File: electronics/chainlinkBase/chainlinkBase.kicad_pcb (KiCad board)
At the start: 2 copper layers, 107 parts, among them J1 Power In, J10 UART, J11 Output, J12 Output, J13 Output, J14 CHANNEL, J2 CHANNEL, J3 CHANNEL, J4 RELAY, J5 CHANNEL, J6 CHANNEL, J7 RS485, J8 RS485, J9 Logic Power Out, SW1 SW_DIP_x04, U1 AP7361C-33E, U10 INA219BxD, U11 VN7007ALH, U12 VN7007ALH, U13 SN74LV1T34DBV, U14 SP485, U15 INA219BxD, U16 VN7007ALH, U17 SN74LV1T34DBV, U2 TPL7407L, U3 INA219BxD, U4 INA219BxD, U5 VN7007ALH, U6 VN7007ALH, U7 TTGO_TDisplay, U8 MCP23017_SS, U9 INA219BxD

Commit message: Single channel layout
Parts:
- removed C10, C11, C12, C15, C16, C23, C5, C6, C7, C8, C9: 0.1uF, Capacitor_SMD:C_0805_2012Metric
- removed D1, D12, D13, D14, D15, D16, D2, D3, D4, D5: Red, LED_SMD:LED_0805_2012Metric
- removed D6, D7: WS2812B, LED_SMD:LED_WS2812B_PLCC4_5.0x5.0mm_P3.2mm
- removed F1, F2, F3, F4, F5: Fuse Holder BK-6013, BK-6013:BK-6013
- removed J1: Power In, ScrewTerminals:EB147A-02-D
- removed J10: UART, ScrewTerminals:C72334_WJ500V-5.08-3P
- removed J11, J12, J13: Output, ScrewTerminals:EB147A-02-D
- removed J14, J2, J3, J5, J6: CHANNEL, ScrewTerminals:EB147A-02-D
- removed J7, J8: RS485, ScrewTerminals:EB147A-02-D
- removed J9: Logic Power Out, ScrewTerminals:EB147A-02-D
- removed R1, R14, R15, R2, R24: 0.01R 1% 1W, Resistor_SMD:R_0612_1632Metric
- removed R10, R20, R21, R27, R9: 220, Resistor_SMD:R_0805_2012Metric
- removed R11, R12, R22, R23, R28: 1k, Resistor_SMD:R_0805_2012Metric
- removed R16, R17, R18, R19, R25, R26, R3, R4, R7, R8: 15k, Resistor_SMD:R_0805_2012Metric
- removed R29, R30, R31, R32, R33: 2k, Resistor_SMD:R_0805_2012Metric
- removed SW1: SW_DIP_x04, Button_Switch_SMD:SW_DIP_SPSTx04_Slide_Omron_A6S-410x_W8.9mm_P2.54mm
- removed U1: AP7361C-33E, Package_TO_SOT_SMD:SOT-223-3_TabPin2
- removed U10, U15, U3, U4, U9: INA219BxD, Package_SO:SOIC-8_3.9x4.9mm_P1.27mm
- removed U11, U12, U16, U5, U6: VN7007ALH, VN7007ALHTR:VN7007ALHTR
- removed U13, U17: SN74LV1T34DBV, Package_TO_SOT_SMD:SOT-23-5
- removed U14: SP485, Package_SO:SOIC-8_3.9x4.9mm_P1.27mm
- removed U8: MCP23017_SS, Package_SO:SSOP-28_5.3x10.2mm_P0.65mm
- added C101: 47uF, Capacitor_SMD:CP_Elec_6.3x5.4, F.Cu at (123.8, 127.6)
- added C104: 47uF, Capacitor_SMD:CP_Elec_6.3x5.4, F.Cu at (123.8, 148.6)
- added C113: 0.1uF, Capacitor_SMD:C_0805_2012Metric, F.Cu at (150.5, 45.1)
- added C201: 0.1uF, Capacitor_SMD:C_0805_2012Metric, F.Cu at (171.4, 47.0)
- added C202: 0.1uF, Capacitor_SMD:C_0805_2012Metric, F.Cu at (174.6, 26.0)
- added D101: WS2812B, LED_SMD:LED_WS2812B_PLCC4_5.0x5.0mm_P3.2mm, F.Cu at (126.4, 165.7)
- added D102: WS2812B, LED_SMD:LED_WS2812B_PLCC4_5.0x5.0mm_P3.2mm, F.Cu at (226.8, 48.5)
- added D107: 2A 500mV, Diode_SMD:D_SOD-128, F.Cu at (129.5, 45.7)
- added D201: Red, LED_SMD:LED_0805_2012Metric, F.Cu at (191.8, 41.9)
- added D202: Red, LED_SMD:LED_0805_2012Metric, F.Cu at (191.8, 29.2)
- added F201: Fuse Holder BK-6013, BK-6013:BK-6013, F.Cu at (181.6, 47.0)
- added H101: MountingHole_Pad, MountingHole:MountingHole_3.2mm_M3_ISO7380_Pad, F.Cu at (105.4, 20.3)
- added H102: MountingHole_Pad, MountingHole:MountingHole_3.2mm_M3_ISO7380_Pad, F.Cu at (193.0, 20.3)
- added H103: MountingHole_Pad, MountingHole:MountingHole_3.2mm_M3_ISO7380_Pad, F.Cu at (193.0, 195.6)
- added H104: MountingHole_Pad, MountingHole:MountingHole_3.2mm_M3_ISO7380_Pad, F.Cu at (104.1, 168.9)
- added J101: Power In, ScrewTerminals:Generic-5.08-2P, F.Cu at (110.5, 40.6)
- added J103: Power In, ScrewTerminals:Generic-5.08-2P, F.Cu at (110.5, 27.9)
- added J104: RS485, ScrewTerminals:Generic-5.08-2P, F.Cu at (109.9, 105.4)
- added J105: RS485, ScrewTerminals:Generic-5.08-2P, F.Cu at (109.9, 115.6)
- added J106: Logic Power Out, ScrewTerminals:Generic-5.08-2P, F.Cu at (110.5, 128.3)
- added J107: UART, ScrewTerminals:Generic-5.08-3P, F.Cu at (109.9, 90.2)
- added J108: Output, ScrewTerminals:Generic-5.08-2P, F.Cu at (110.5, 141.0)
- added J109: Output, ScrewTerminals:Generic-5.08-2P, F.Cu at (110.5, 151.1)
- added J110: Output, ScrewTerminals:Generic-5.08-2P, F.Cu at (110.5, 161.3)
- added J201: CHANNEL, ScrewTerminals:Generic-5.08-2P, F.Cu at (184.2, 38.1)
- added JP101: LEDs, Connector_PinHeader_2.54mm:PinHeader_1x02_P2.54mm_Vertical, F.Cu at (188.0, 21.6)
- added R201: 0.01R 1% 1W, Resistor_SMD:R_0612_1632Metric, F.Cu at (174.0, 38.1)
- added R202: 2k, Resistor_SMD:R_0805_2012Metric, F.Cu at (191.8, 44.5)
- added R203: 15k, Resistor_SMD:R_0805_2012Metric, F.Cu at (184.2, 28.6)
- added R204: 15k, Resistor_SMD:R_0805_2012Metric, F.Cu at (179.7, 26.0)
- added R205: 2k, Resistor_SMD:R_0805_2012Metric, F.Cu at (191.8, 26.7)
- added R206: 1k, Resistor_SMD:R_0805_2012Metric, F.Cu at (179.7, 28.6)
- added SW101: SW_DIP_x04, Button_Switch_SMD:SW_DIP_SPSTx04_Slide_Omron_A6S-410x_W8.9mm_P2.54mm, F.Cu at (110.5, 77.5)
- added U101: AP7361C-33E, Package_TO_SOT_SMD:SOT-223-3_TabPin2, F.Cu at (123.8, 137.2)
- added U103: Buck, Buck:BuckModule, F.Cu at (136.5, 25.4)
- added U105: MCP23017_SS, Package_SO:SSOP-28_5.3x10.2mm_P0.65mm, F.Cu at (122.6, 74.3)
- added U106: SN74LV1T34DBV, Package_TO_SOT_SMD:SOT-23-5, F.Cu at (125.7, 109.2)
- added U107: SP485, Package_SO:SOIC-8_3.9x4.9mm_P1.27mm, F.Cu at (132.1, 97.2)
- added U108: SN74LV1T34DBV, Package_TO_SOT_SMD:SOT-23-5, F.Cu at (132.9, 166.1)
- added U201: INA219BxD, Package_SO:SOIC-8_3.9x4.9mm_P1.27mm, F.Cu at (166.4, 45.7)
- added U202: VN7007ALH, VN7007ALHTR:VN7007ALHTR, F.Cu at (168.9, 31.1)
- J102: renamed from J4; footprint ScrewTerminals:EB147A-02-D -> ScrewTerminals:Generic-5.08-2P
- moved C106 223.5 mm to (257.0, 109.2)
- moved C111 223.5 mm to (263.4, 93.8)
- moved C102 209.3 mm to (264.8, 74.3)
- moved C103 209.3 mm to (241.8, 93.8)
- moved C105 209.3 mm to (269.2, 75.7)
- moved C107 209.3 mm to (252.3, 89.2)
- moved C108 209.3 mm to (264.8, 77.3)
- moved C109 209.3 mm to (239.0, 102.8)
- moved C110 209.3 mm to (260.9, 80.3)
- moved C112 209.3 mm to (239.0, 99.8)
- moved D103 209.3 mm to (253.9, 76.7)
- moved D104 209.3 mm to (245.5, 76.7)
- moved D105 209.3 mm to (255.3, 68.4)
- moved R101 209.3 mm to (261.2, 89.3)
- moved R102 209.3 mm to (247.9, 102.8)
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- renumbered C2 to C102, C3 to C103, C13 to C105, C14 to C106, C17 to C107, C18 to C108, C19 to C109, C20 to C110, C21 to C111, C22 to C112, D8 to D103, D9 to D104, D10 to D105, D11 to D106, R5 to R101, R6 to R102, R13 to R103, U2 to U102, U7 to U104
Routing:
- net /OUT0_EN: track 0.00 -> 49.4 mm
- net GND: track 0.00 -> 36.6 mm, vias 0 -> 3
- net /LED_GND: track 0.00 -> 36.4 mm
- net Net-(D201-Pad2): track 0.00 -> 29.4 mm
- net +3V3: track 0.00 -> 26.5 mm
- net /PowerChannel0/POWER_MONITORED: track 0.00 -> 22.7 mm, vias 0 -> 30
- net Net-(D105-Pad2): track 0.00 -> 19.8 mm
- net /SCL: track 0.00 -> 18.5 mm
- net /SDA: track 0.00 -> 17.7 mm
- net Net-(R203-Pad1): track 0.00 -> 9.95 mm
- net +5V: track 0.00 -> 9.56 mm
- net (no net): track 0.00 -> 9.31 mm
- net /PowerChannel0/POWER_OUT: track 0.00 -> 8.26 mm
- net Net-(R204-Pad2): track 0.00 -> 6.02 mm
- net Net-(R206-Pad2): track 0.00 -> 5.16 mm
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- added copper zone on B.Cu, net (none)
- added copper zone on F.Cu, net /PowerChannel0/POWER_IN
- added copper zone on F.Cu, net /PowerChannel0/POWER_MONITORED
- added copper zone on F.Cu, net /PowerChannel0/POWER_OUT
- added copper zone on B.Cu, net GND
- added copper zone on F.Cu, net Net-(D201-Pad2)
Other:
- board outline added: 94.6 x 182.2 mm
- rule trace_min: 0.2 -> 0.16
- board text added: "Channel 0"
- board text added: "In"
- board text added: "LEDs"
- board text added: "Out"

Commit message: Lots of layout and routing
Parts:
- added C114: 0.1uF, Capacitor_SMD:C_0805_2012Metric, F.Cu at (47.6, 81.9)
- added C301: 0.1uF, Capacitor_SMD:C_0805_2012Metric, F.Cu at (99.1, 87.6)
- added C302: 0.1uF, Capacitor_SMD:C_0805_2012Metric, F.Cu at (102.2, 66.7)
- added C401: 0.1uF, Capacitor_SMD:C_0805_2012Metric, F.Cu at (99.1, 120.0)
- added C402: 0.1uF, Capacitor_SMD:C_0805_2012Metric, F.Cu at (102.2, 99.1)
- added C501: 0.1uF, Capacitor_SMD:C_0805_2012Metric, F.Cu at (99.1, 152.4)
- added C502: 0.1uF, Capacitor_SMD:C_0805_2012Metric, F.Cu at (102.2, 131.4)
- added C601: 0.1uF, Capacitor_SMD:C_0805_2012Metric, F.Cu at (99.1, 184.8)
- added C602: 0.1uF, Capacitor_SMD:C_0805_2012Metric, F.Cu at (102.2, 163.8)
- added D301: Red, LED_SMD:LED_0805_2012Metric, F.Cu at (119.4, 82.5)
- added D302: Red, LED_SMD:LED_0805_2012Metric, F.Cu at (119.4, 69.8)
- added D401: Red, LED_SMD:LED_0805_2012Metric, F.Cu at (119.4, 114.9)
- added D402: Red, LED_SMD:LED_0805_2012Metric, F.Cu at (119.4, 102.2)
- added D501: Red, LED_SMD:LED_0805_2012Metric, F.Cu at (119.4, 147.3)
- added D502: Red, LED_SMD:LED_0805_2012Metric, F.Cu at (119.4, 134.6)
- added D601: Red, LED_SMD:LED_0805_2012Metric, F.Cu at (119.4, 179.7)
- added D602: Red, LED_SMD:LED_0805_2012Metric, F.Cu at (119.4, 167.0)
- added F301: Fuse Holder BK-6013, BK-6013:BK-6013, F.Cu at (109.2, 87.6)
- added F401: Fuse Holder BK-6013, BK-6013:BK-6013, F.Cu at (109.2, 120.0)
- added F501: Fuse Holder BK-6013, BK-6013:BK-6013, F.Cu at (109.2, 152.4)
- added F601: Fuse Holder BK-6013, BK-6013:BK-6013, F.Cu at (109.2, 184.8)
- added J111: Conn_01x06_Male, Connector_PinHeader_2.54mm:PinHeader_1x06_P2.54mm_Vertical, F.Cu at (48.9, 59.1)
- added J112: Conn_01x06_Male, Connector_PinHeader_2.54mm:PinHeader_1x06_P2.54mm_Vertical, F.Cu at (51.4, 59.1)
- added J301: CHANNEL, ScrewTerminals:Generic-5.08-2P, F.Cu at (111.8, 78.7)
- added J401: CHANNEL, ScrewTerminals:Generic-5.08-2P, F.Cu at (111.8, 111.1)
- added J501: CHANNEL, ScrewTerminals:Generic-5.08-2P, F.Cu at (111.8, 143.5)
- added J601: CHANNEL, ScrewTerminals:Generic-5.08-2P, F.Cu at (111.8, 175.9)
- added R301: 0.01R 1% 1W, Resistor_SMD:R_0612_1632Metric, F.Cu at (101.6, 78.7)
- added R302: 2k, Resistor_SMD:R_0805_2012Metric, F.Cu at (119.4, 85.1)
- added R303: 15k, Resistor_SMD:R_0805_2012Metric, F.Cu at (111.8, 69.2)
- added R304: 15k, Resistor_SMD:R_0805_2012Metric, F.Cu at (107.3, 66.7)
- added R305: 2k, Resistor_SMD:R_0805_2012Metric, F.Cu at (119.4, 67.3)
- added R306: 1k, Resistor_SMD:R_0805_2012Metric, F.Cu at (107.3, 69.2)
- added R401: 0.01R 1% 1W, Resistor_SMD:R_0612_1632Metric, F.Cu at (101.6, 111.1)
- added R402: 2k, Resistor_SMD:R_0805_2012Metric, F.Cu at (119.4, 117.5)
- added R403: 15k, Resistor_SMD:R_0805_2012Metric, F.Cu at (111.8, 101.6)
- added R404: 15k, Resistor_SMD:R_0805_2012Metric, F.Cu at (107.3, 99.1)
- added R405: 2k, Resistor_SMD:R_0805_2012Metric, F.Cu at (119.4, 99.7)
- added R406: 1k, Resistor_SMD:R_0805_2012Metric, F.Cu at (107.3, 101.6)
- added R501: 0.01R 1% 1W, Resistor_SMD:R_0612_1632Metric, F.Cu at (101.6, 143.5)
- added R502: 2k, Resistor_SMD:R_0805_2012Metric, F.Cu at (119.4, 149.9)
- added R503: 15k, Resistor_SMD:R_0805_2012Metric, F.Cu at (111.8, 134.0)
- added R504: 15k, Resistor_SMD:R_0805_2012Metric, F.Cu at (107.3, 131.4)
- added R505: 2k, Resistor_SMD:R_0805_2012Metric, F.Cu at (119.4, 132.1)
- added R506: 1k, Resistor_SMD:R_0805_2012Metric, F.Cu at (107.3, 134.0)
- added R601: 0.01R 1% 1W, Resistor_SMD:R_0612_1632Metric, F.Cu at (101.6, 175.9)
- added R602: 2k, Resistor_SMD:R_0805_2012Metric, F.Cu at (119.4, 182.2)
- added R603: 15k, Resistor_SMD:R_0805_2012Metric, F.Cu at (111.8, 166.4)
- added R604: 15k, Resistor_SMD:R_0805_2012Metric, F.Cu at (107.3, 163.8)
- added R605: 2k, Resistor_SMD:R_0805_2012Metric, F.Cu at (119.4, 164.5)
- added R606: 1k, Resistor_SMD:R_0805_2012Metric, F.Cu at (107.3, 166.4)
- added U301: INA219BxD, Package_SO:SOIC-8_3.9x4.9mm_P1.27mm, F.Cu at (94.0, 86.4)
- added U302: VN7007ALH, VN7007ALHTR:VN7007ALHTR, F.Cu at (96.5, 71.8)
- added U401: INA219BxD, Package_SO:SOIC-8_3.9x4.9mm_P1.27mm, F.Cu at (94.0, 118.7)
- added U402: VN7007ALH, VN7007ALHTR:VN7007ALHTR, F.Cu at (96.5, 104.1)
- added U501: INA219BxD, Package_SO:SOIC-8_3.9x4.9mm_P1.27mm, F.Cu at (94.0, 151.1)
- added U502: VN7007ALH, VN7007ALHTR:VN7007ALHTR, F.Cu at (96.5, 136.5)
- added U601: INA219BxD, Package_SO:SOIC-8_3.9x4.9mm_P1.27mm, F.Cu at (94.0, 183.5)
- added U602: VN7007ALH, VN7007ALHTR:VN7007ALHTR, F.Cu at (96.5, 168.9)
- moved R101 253.5 mm to (39.4, 212.1), turned to 90 degrees
- moved C108 232.0 mm to (52.7, 171.4), turned to 270 degrees
- moved R102 230.9 mm to (44.5, 212.1), turned to 90 degrees
- moved C107 223.8 mm to (47.6, 179.7), turned to 270 degrees
- moved C102 220.0 mm to (54.0, 137.2)
- moved C105 217.6 mm to (56.5, 121.3), turned to 90 degrees
- moved C106 207.9 mm to (49.5, 121.3), turned to 180 degrees
- moved D102 196.2 mm to (84.5, 183.5)
- moved C110 195.8 mm to (78.1, 150.5), turned to 270 degrees
- moved C103 195.1 mm to (54.0, 146.7)
- moved R103 189.3 mm to (59.1, 87.0), turned to 180 degrees
- moved C111 186.9 mm to (78.1, 118.1), turned to 270 degrees
- moved D103 185.1 mm to (84.5, 151.1)
- moved C109 179.7 mm to (78.1, 182.9), turned to 270 degrees
- moved D105 171.8 mm to (84.5, 86.4)
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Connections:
- H101 pad 1: (no net) -> GND
- H102 pad 1: (no net) -> GND
- H103 pad 1: (no net) -> GND
- H104 pad 1: (no net) -> GND
- U102 pad 10: (no net) -> Net-(J111-Pad1)
- U102 pad 11: (no net) -> Net-(J111-Pad2)
- U102 pad 12: (no net) -> Net-(J111-Pad3)
- U102 pad 13: (no net) -> Net-(J111-Pad4)
- U102 pad 14: (no net) -> Net-(J111-Pad5)
- U102 pad 15: (no net) -> Net-(J111-Pad6)
- U102 pad 2: (no net) -> /MISC0
- U102 pad 3: (no net) -> /MISC1
- U102 pad 4: (no net) -> /MISC2
- U102 pad 5: (no net) -> /MISC3
- U102 pad 6: (no net) -> /MISC4
- U102 pad 7: GND -> /MISC5
- U105 pad 1: /OUT0_EN -> /MISC5
- U105 pad 2: /OUT1_EN -> /MISC4
- U105 pad 22: (no net) -> /OUT4_EN
- U105 pad 23: (no net) -> /OUT3_EN
- U105 pad 24: (no net) -> /OUT2_EN
- U105 pad 25: /ADDR_0 -> /OUT1_EN
- U105 pad 26: /ADDR_1 -> /OUT0_EN
- U105 pad 27: /ADDR_2 -> /MISC1
- U105 pad 28: /ADDR_3 -> /MISC0
- U105 pad 3: /OUT2_EN -> /MISC3
- U105 pad 4: /OUT3_EN -> /MISC2
- U105 pad 5: /OUT4_EN -> /ADDR_3
- U105 pad 6: (no net) -> /ADDR_2
- U105 pad 7: (no net) -> /ADDR_1
- U105 pad 8: (no net) -> /ADDR_0
- U107 pad 6: Net-(J104-Pad2) -> Net-(J104-Pad1)
- U107 pad 7: Net-(J104-Pad1) -> Net-(J104-Pad2)
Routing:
- net +5V: track 9.56 -> 411.4 mm, vias 0 -> 10
- net +3V3: track 26.5 -> 402.1 mm, vias 0 -> 2
- net /SDA: track 17.7 -> 313.3 mm, vias 0 -> 11
- net /SCL: track 18.5 -> 312.7 mm, vias 0 -> 11
- net GND: track 36.6 -> 252.3 mm, vias 3 -> 26
- net /LED_GND: track 36.4 -> 203.4 mm
- net /OUT4_EN: track 0.00 -> 137.2 mm, vias 0 -> 2
- net /OUT3_EN: track 0.00 -> 106.2 mm, vias 0 -> 2
- net /OUT1_EN: track 0.00 -> 73.1 mm, vias 0 -> 2
- net /OUT2_EN: track 0.00 -> 72.9 mm, vias 0 -> 2
- net Net-(D104-Pad2): track 0.00 -> 69.9 mm, vias 0 -> 4
- net Net-(D102-Pad2): track 0.00 -> 69.8 mm, vias 0 -> 4
- net Net-(D103-Pad2): track 0.00 -> 69.3 mm, vias 0 -> 4
- net /OUT0_EN: track 49.4 -> 106.1 mm, vias 0 -> 2
- net Net-(D105-Pad2): track 19.8 -> 68.9 mm, vias 0 -> 4
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- added copper zone on B.Cu, net /PowerChannel0/POWER_MONITORED
- added copper zone on F.Cu, net /PowerChannel1/POWER_IN
- added copper zone on B.Cu, net /PowerChannel1/POWER_MONITORED
- added copper zone on F.Cu, net /PowerChannel1/POWER_MONITORED
- added copper zone on F.Cu, net /PowerChannel1/POWER_OUT
- added copper zone on F.Cu, net /PowerChannel2/POWER_IN
- added copper zone on B.Cu, net /PowerChannel2/POWER_MONITORED
- added copper zone on F.Cu, net /PowerChannel2/POWER_MONITORED
- added copper zone on F.Cu, net /PowerChannel2/POWER_OUT
- added copper zone on F.Cu, net /PowerChannel3/POWER_IN
- added copper zone on B.Cu, net /PowerChannel3/POWER_MONITORED
- added copper zone on F.Cu, net /PowerChannel3/POWER_MONITORED
- added copper zone on F.Cu, net /PowerChannel3/POWER_OUT
- added copper zone on F.Cu, net /PowerChannel4/POWER_IN
- added copper zone on B.Cu, net /PowerChannel4/POWER_MONITORED
- added copper zone on F.Cu, net /PowerChannel4/POWER_MONITORED
- added copper zone on F.Cu, net /PowerChannel4/POWER_OUT
- added copper zone on F.Cu, net Net-(D301-Pad2)
- added copper zone on F.Cu, net Net-(D401-Pad2)
- added copper zone on F.Cu, net Net-(D501-Pad2)
- added copper zone on F.Cu, net Net-(D601-Pad2)
- removed copper zone on B.Cu, net (none)
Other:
- board size 94.6 x 182.2 mm -> 98.4 x 190.5 mm
- board text added: "1"
- board text added: "12V"
- board text added: "2"
- board text added: "3.3V"
- board text added: "4"
- board text added: "500mA Max"
- board text added: "5V"
- board text added: "8"
- board text added: "A"
- board text added: "Address"
- board text added: "B"
- board text added: "CLK"
- board text added: "Channel 1"
- board text added: "Channel 2"
- board text added: "Channel 3"
- board text added: "Channel 4"
- board text added: "DATE: YYYY-MM-DD COMMIT: deadbeef"
- board text added: "GND"
- board text added: "MD"
- board text added: "ML"
- board text added: "Next/Up"
- board text added: "Output"
- board text added: "Power In"
- board text added: "Pwr Out"
- board text added: "RS485"
- board text added: "RX"
- board text added: "Relay"
- board text added: "Reset"
- board text added: "SD"
- board text added: "SHD"
- board text added: "Select"
- board text added: "Splitflap Chainlink Base"
- board text added: "Status"
- board text added: "TX"
- board text added: "UART"
- board text added: "https://github.com/scottbez1/splitflap"

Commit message: More routing, CI
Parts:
- U103: footprint Buck:BuckModule -> Buck:BuckModuleBackSilk
- moved C108 8.82 mm to (60.3, 175.9), turned to 180 degrees
- moved C105 6.38 mm to (57.1, 114.9), turned to 180 degrees
- moved U106 4.96 mm to (57.1, 118.1), turned to 0 degrees
- moved U103 2.29 mm to (66.0, 32.4)
- moved D107 2.01 mm to (59.1, 55.9)
- moved C104 1.27 mm to (54.0, 151.8)
- moved C106 1.27 mm to (49.5, 120.0)
- moved C101 0.64 mm to (54.0, 131.4)
- moved C102 0.63 mm to (54.0, 136.5)
- turned D101 to 180 degrees
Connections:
- J107 pad 1: /TX -> /RX
- J107 pad 2: /RX -> /TX
- U104 pad 24: +3V3 -> (no net)
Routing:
- net /MASTER_EN: track 0.00 -> 168.6 mm, vias 0 -> 2
- net /TX: track 0.00 -> 152.3 mm, vias 0 -> 2
- net /RX: track 0.00 -> 152.0 mm, vias 0 -> 2
- net /MCP_INT: track 0.00 -> 144.9 mm
- net /MCP_RESET: track 0.00 -> 127.5 mm
- net /RS485_DRIVE_EN: track 0.00 -> 124.2 mm, vias 0 -> 2
- net +5V: track 411.4 -> 470.4 mm, vias 10 -> 11
- net GND: track 252.3 -> 273.7 mm, vias 26 -> 33
- net Net-(J104-Pad2): track 0.00 -> 21.4 mm
- net Net-(J104-Pad1): track 0.00 -> 21.2 mm
- net Net-(D101-Pad2): track 24.8 -> 45.2 mm
- net +3V3: track 402.1 -> 418.4 mm, vias 2 -> 4
- net /RGB_LEDS: track 0.00 -> 6.67 mm
- net /RGB_LEDS_3V3: track 0.00 -> 5.14 mm
- net Net-(U106-Pad2): track 0.00 -> 2.77 mm
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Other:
- board text added: "7V to 28V"
- board text removed: "12V"

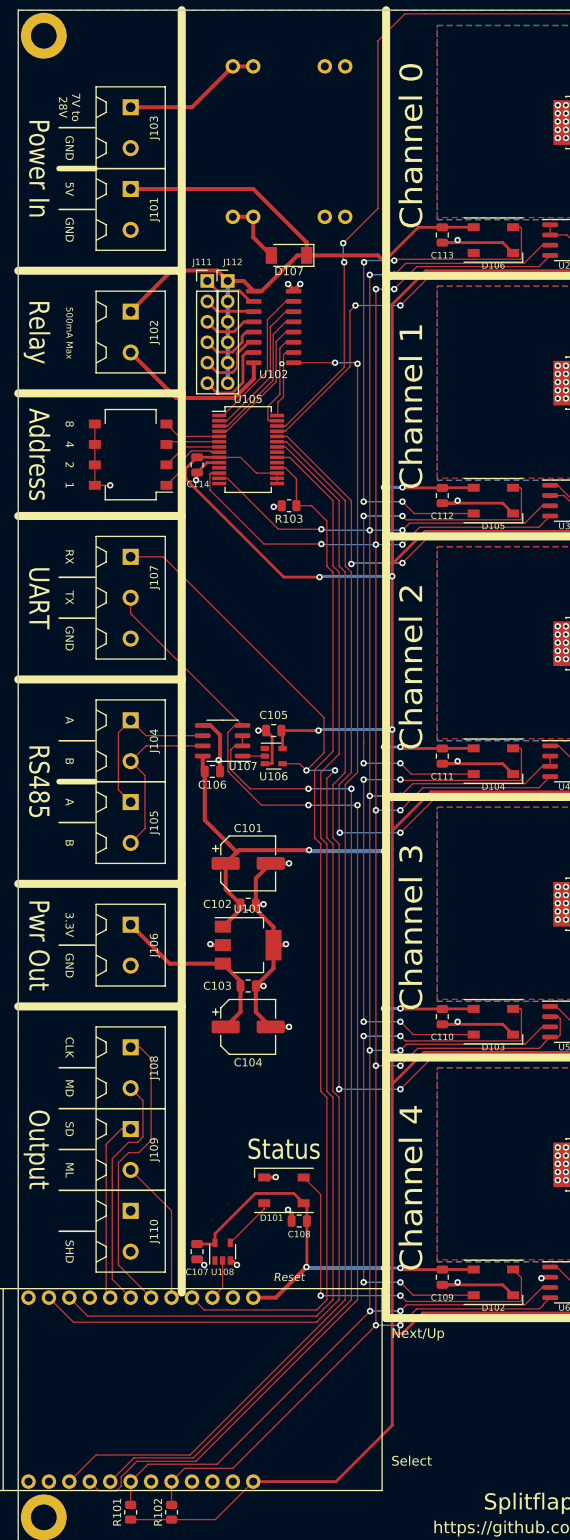
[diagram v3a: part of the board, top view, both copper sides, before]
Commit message: Chainlink Base - Digikey part numbers, schematic cleanup, minor pcb tweaks
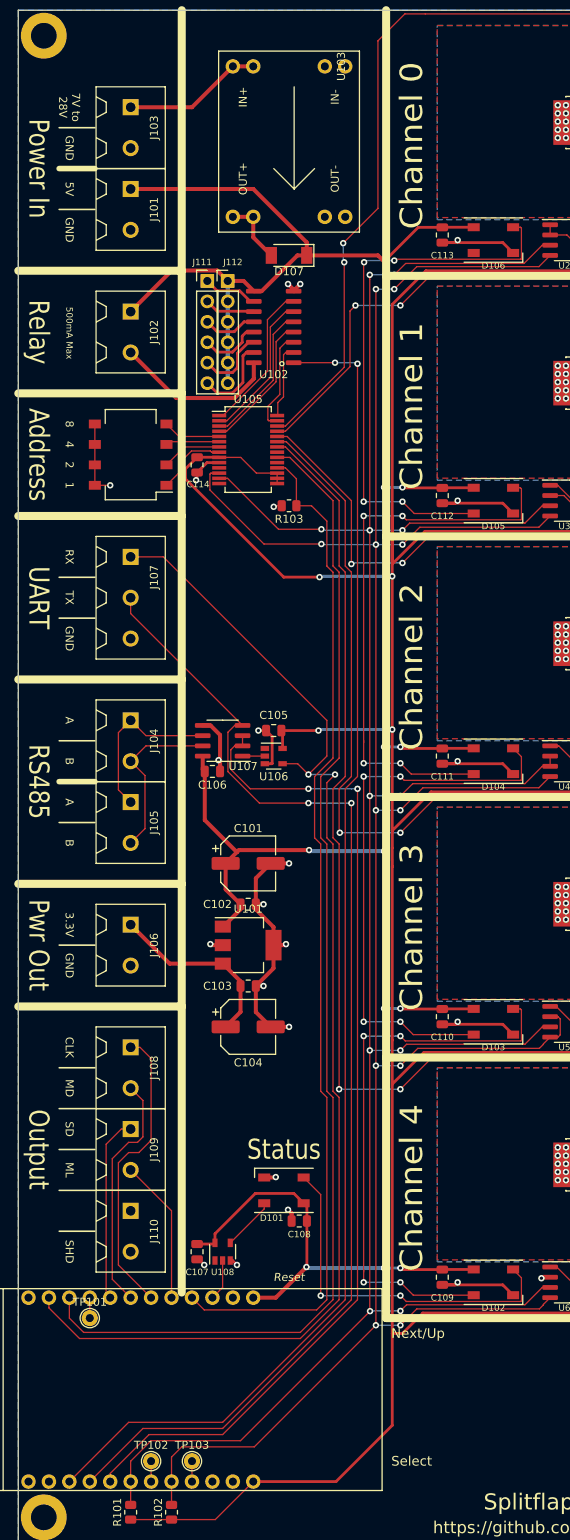
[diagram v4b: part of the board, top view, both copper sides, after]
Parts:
- added TP101: TestPoint_Small, TestPoint:TestPoint_THTPad_D2.0mm_Drill1.0mm, F.Cu at (34.3, 188.0)
- added TP102: TestPoint_Small, TestPoint:TestPoint_THTPad_D2.0mm_Drill1.0mm, F.Cu at (41.9, 205.7)
- added TP103: TestPoint_Small, TestPoint:TestPoint_THTPad_D2.0mm_Drill1.0mm, F.Cu at (47.0, 205.7)
- added Z201: Fuse, Dummy:Dummy, F.Cu at (143.5, 43.7)
- added Z301: Fuse, Dummy:Dummy, F.Cu at (159.0, 33.6)
- added Z401: Fuse, Dummy:Dummy, F.Cu at (149.2, 43.7)
- added Z501: Fuse, Dummy:Dummy, F.Cu at (159.0, 38.2)
- added Z601: Fuse, Dummy:Dummy, F.Cu at (164.7, 33.6)
- R103: value 10k -> 15k
- U103: footprint Buck:BuckModuleBackSilk -> Buck:BuckModule
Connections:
- U104 pad 21: (no net) -> Net-(TP101-Pad1)
- U104 pad 7: (no net) -> Net-(TP102-Pad1)
- U104 pad 9: (no net) -> Net-(TP103-Pad1)
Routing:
- net /MCP_INT: track 144.9 -> 148.1 mm
- net /TX: track 152.3 -> 149.3 mm
- net /RX: track 152.0 -> 154.8 mm
- net Net-(TP101-Pad1): track 0.00 -> 2.54 mm
- net Net-(TP103-Pad1): track 0.00 -> 2.54 mm
- net Net-(TP102-Pad1): track 0.00 -> 2.54 mm
- net /RS485_DRIVE_EN: track 124.2 -> 126.3 mm
- net /SCL: track 312.7 -> 314.4 mm
- net /SDA: track 312.1 -> 313.6 mm
